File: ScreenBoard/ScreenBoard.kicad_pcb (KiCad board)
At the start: 4 copper layers, 39.8 x 35.6 mm, 23 parts, among them IC1 FAN5331SX, J1 Micro_SD_Card, J2 Conn_02x05_Male, K1 OLED connector

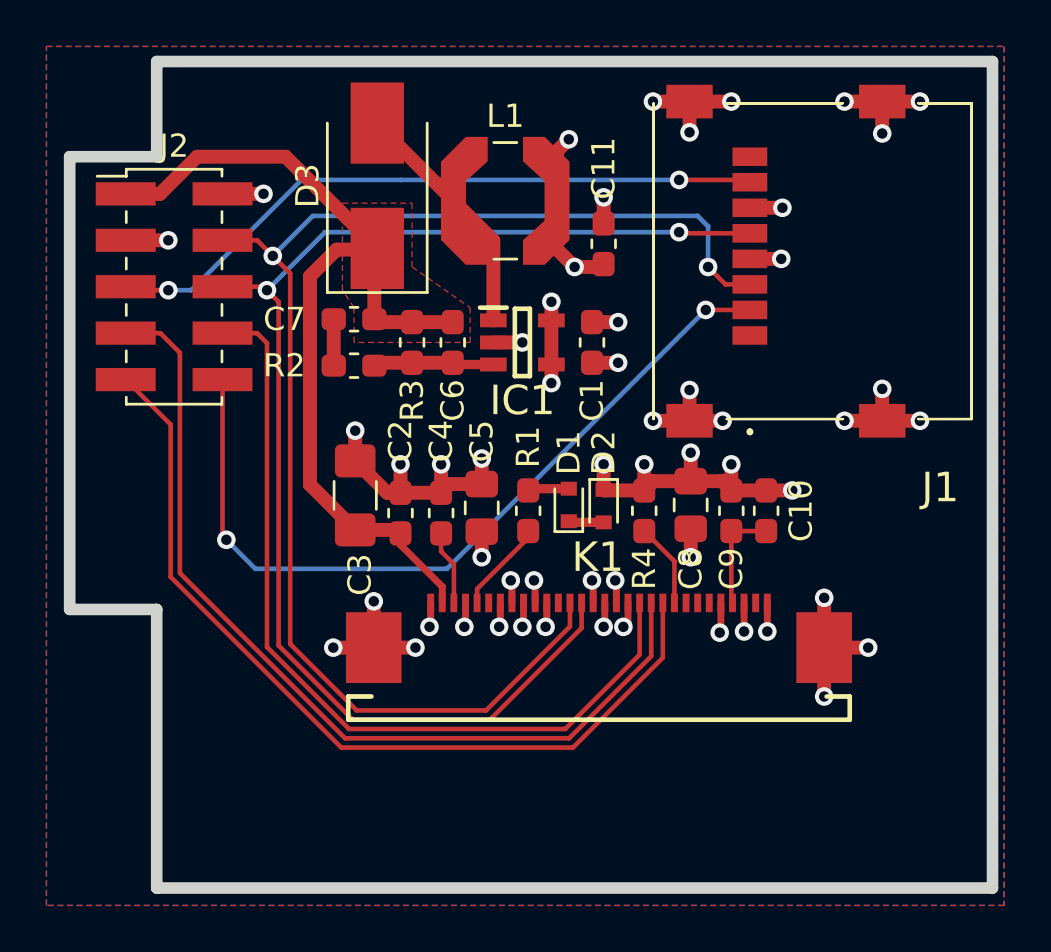
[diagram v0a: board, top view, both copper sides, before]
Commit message: Change C11 footprint for better component availability
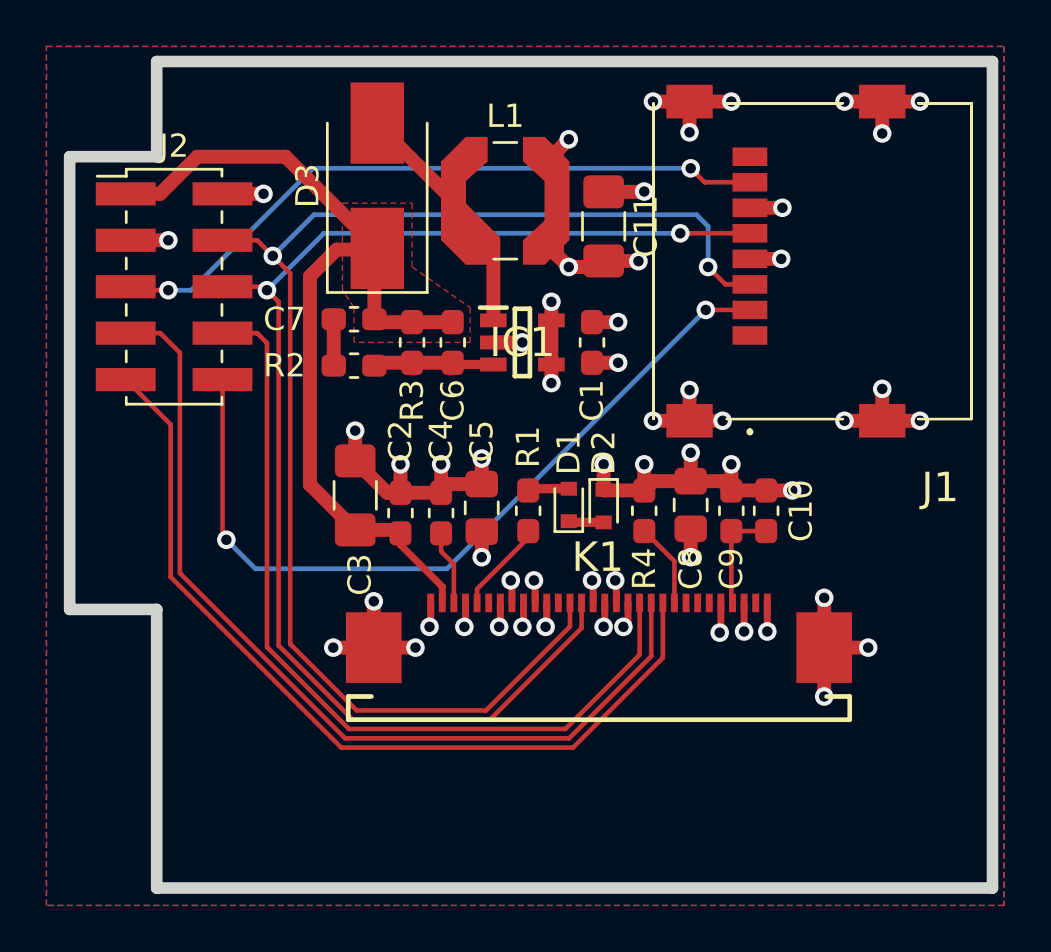
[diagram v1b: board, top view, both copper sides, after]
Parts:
- C11: footprint Capacitor_SMD:C_0603_1608Metric_Pad1.05x0.95mm_HandSolder -> Capacitor_SMD:C_1206_3216Metric_Pad1.42x1.75mm_HandSolder
- moved C11 0.75 mm to (121.8, 55.5)
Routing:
- net +3V3: track 19.7 -> 21.5 mm, vias 11 -> 12
- net GND: track 75.5 -> 76.2 mm

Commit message: Merge display shield and update smd components case
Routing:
- added copper zone on In2.Cu, net +3V3
- added copper zone on In1.Cu, net GND
- removed copper zone on In2_+3.3V.Cu, net +3V3
- removed copper zone on In1_GND.Cu, net GND
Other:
- net class Default removed
- net class power removed
